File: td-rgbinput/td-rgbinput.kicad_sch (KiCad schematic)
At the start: 52 parts, among them J1 Conn_01x06_Male, J2 Conn_01x07_Male, J3 Conn_01x06_Male, J5 DB15_Female_HighDensity_Mount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, SW1 SW_DIP_x04, U1 TLC272, U11 LM2664M4, U2 ADP7142AUJZ-5.0, U3 ADA4861-3, U4 74HCT00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

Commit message: fix todos
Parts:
- removed U11: LM2664M4, Package_TO_SOT_SMD:SOT-23-6, symbol td-io:LM2664M4
- removed U2: ADP7142AUJZ-5.0, Package_TO_SOT_SMD:TSOT-23-5, symbol Regulator_Linear:ADP7142AUJZ-5.0
- added C? (x3): 0.1uF, Capacitor_SMD:C_0805_2012Metric, symbol Device:C
- added unit 3 of U1
- added U11: MAX1720EUT, Package_TO_SOT_SMD:SOT-23-6, symbol td-io:MAX1720EUT
- added U?: TLC274, symbol Amplifier_Operational:TLC274
- added U?: ADP7142ARDZ-5.0, Package_SO:SOIC-8-1EP_3.9x4.9mm_P1.27mm_EP2.29x3mm, symbol Regulator_Linear:ADP7142ARDZ-5.0
- added U?: 74HCT00, Package_SO:SOIC-14_3.9x8.7mm_P1.27mm, symbol 74xx:74HC00
- SW1: Digikey CT2064-ND -> CT2194MST-ND
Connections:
- net +12V: now also J3.1 (Pin_1), U?.5 (EN), U?.7 (VIN), U?.8 (VIN); no longer J3.6 (Pin_6)
- net +5V: now also C?.1, C?.1, C?.1, U1.8 (V+), U11.2 (V+), U11.5 (SHDN), U?.1 (VOUT), U?.14 (VCC), U?.2 (VOUT), U?.3 (SENSE/ADJ), U?.4 (V+)
- net -5V: now also RV1.3, C?.2, C?.2, U1.4 (V-), U11.1 (OUT), U?.11 (V-)
- net GND: now also J3.5 (Pin_5), J3.6 (Pin_6), C?.2, U11.4 (GND), U?.4 (GND), U?.7 (GND), U?.9 (GND); no longer J3.1 (Pin_1), J3.2 (Pin_2), RV1.3
- net neck_blue: now also J3.4 (Pin_4); no longer J3.3 (Pin_3)
- net neck_green: now also J3.3 (Pin_3); no longer J3.4 (Pin_4)
- net neck_red: now also J3.2 (Pin_2); no longer J3.5 (Pin_5)
- net at C30.2: now also U11.3 (CAP-)
- net at C30.1: now also U11.6 (CAP+)
- no-connect marks 4 -> 5
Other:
- note removed: "todo: switch gain knob to -5V add power to global opamp add power to 7400 change linear regulator footprint reduce paste on ad8337 reverse pinout on output connector switch digikey pn on dip sw"

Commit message: finish pcb
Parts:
- removed C?: 0.1uF, Capacitor_SMD:C_0805_2012Metric, symbol Device:C
- removed R10: 1k, Resistor_SMD:R_0805_2012Metric, symbol Device:R
- removed RV3: 1k, Potentiometer_THT:Potentiometer_Bourns_3386P_Vertical, symbol Device:R_POT
- removed U?: TLC274, symbol Amplifier_Operational:TLC274
- gave numbers to parts that had none: 4

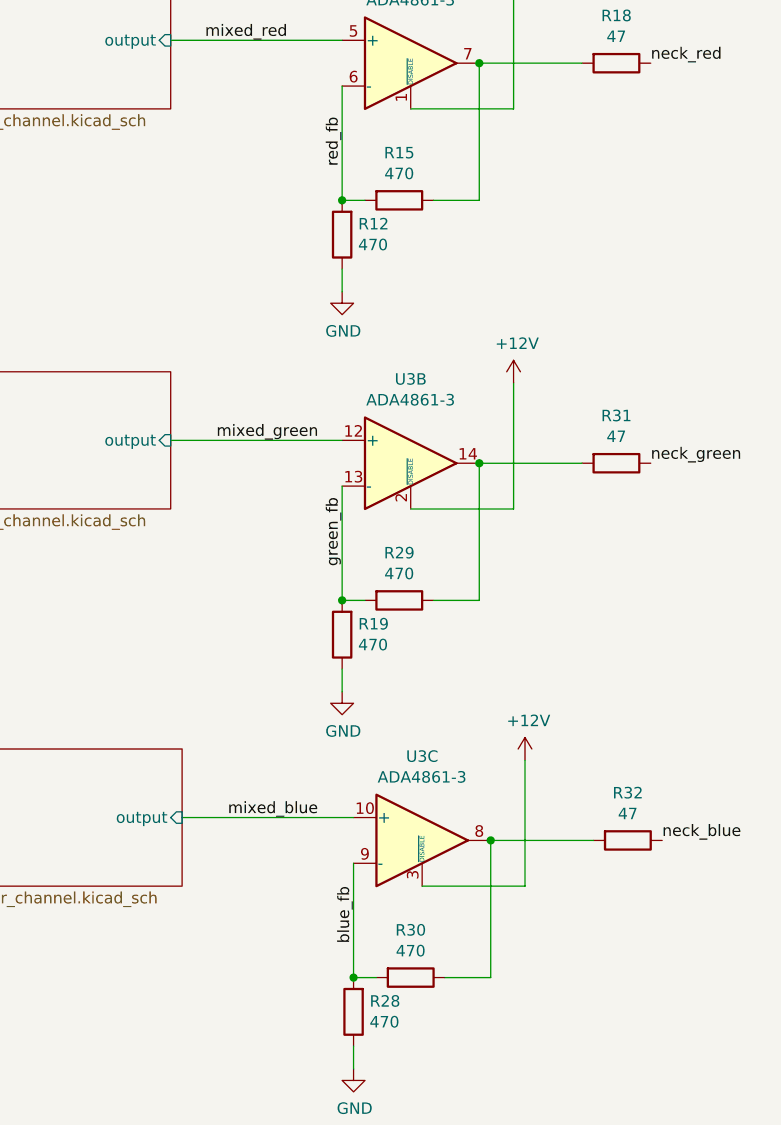
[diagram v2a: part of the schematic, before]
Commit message: update td-rgbinput to reflect constructed circuit
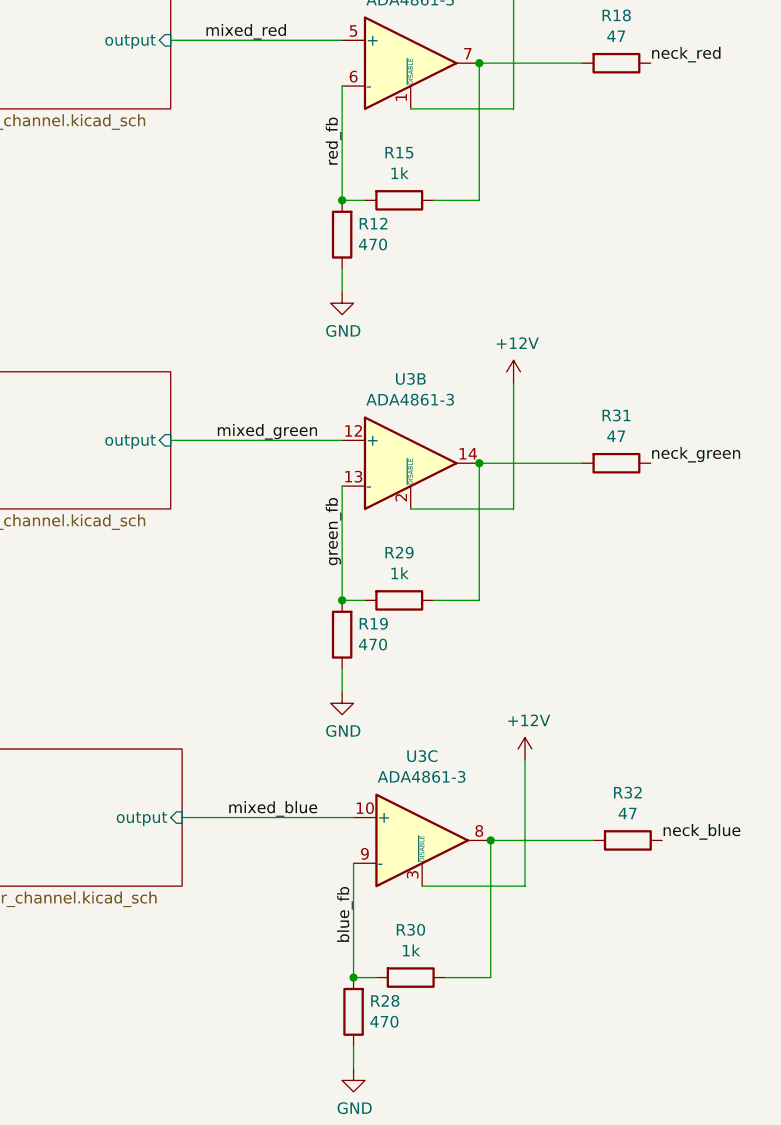
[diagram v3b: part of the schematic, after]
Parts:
- R15, R29, R30: value 470 -> 1k; Digikey YAG3733CT-ND -> (none)
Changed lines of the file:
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@@
     (in_bom yes) (on_board yes)
     (property "Reference" "R15" (id 0) (at 314.96 63.3222 90))
-    (property "Value" "470" (id 1) (at 314.96 65.6336 90))
+    (property "Value" "1k" (id 1) (at 314.96 65.6336 90))
     (property "Footprint" "Resistor_SMD:R_0805_2012Metric" (id 2) (at 314.96 66.802 90)
       (effects (font (size 1.27 1.27)) hide)
@@
       (effects (font (size 1.27 1.27)) hide)
     )
-    (property "Digikey" "YAG3733CT-ND" (id 4) (at 314.96 68.58 0)
+    (property "Digikey" "" (id 4) (at 314.96 68.58 0)
       (effects (font (size 1.27 1.27)) hide)
     )
@@
     (in_bom yes) (on_board yes)
     (property "Reference" "R29" (id 0) (at 314.96 107.7722 90))
-    (property "Value" "470" (id 1) (at 314.96 110.0836 90))
+    (property "Value" "1k" (id 1) (at 314.96 110.0836 90))
     (property "Footprint" "Resistor_SMD:R_0805_2012Metric" (id 2) (at 314.96 111.252 90)
       (effects (font (size 1.27 1.27)) hide)
@@
       (effects (font (size 1.27 1.27)) hide)
     )
-    (property "Digikey" "YAG3733CT-ND" (id 4) (at 314.96 113.03 0)
+    (property "Digikey" "" (id 4) (at 314.96 113.03 0)
       (effects (font (size 1.27 1.27)) hide)
     )
@@
     (in_bom yes) (on_board yes)
     (property "Reference" "R30" (id 0) (at 316.23 149.6822 90))
-    (property "Value" "470" (id 1) (at 316.23 151.9936 90))
+    (property "Value" "1k" (id 1) (at 316.23 151.9936 90))
     (property "Footprint" "Resistor_SMD:R_0805_2012Metric" (id 2) (at 316.23 153.162 90)
       (effects (font (size 1.27 1.27)) hide)
@@
       (effects (font (size 1.27 1.27)) hide)
     )
-    (property "Digikey" "YAG3733CT-ND" (id 4) (at 316.23 154.94 0)
+    (property "Digikey" "" (id 4) (at 316.23 154.94 0)
       (effects (font (size 1.27 1.27)) hide)
     )
@@
       (reference "#PWR0117") (unit 1) (value "+5V") (footprint "")
     )
-    (path "/00000000-0000-0000-0000-0000618fc4a2/9c91e0e5-b30d-4538-ba18-c84d90521e3d"
-      (reference "#PWR0118") (unit 1) (value "GND") (footprint "")
-    )
     (path "/00000000-0000-0000-0000-0000618fc4a2/879ef088-b267-418b-b2b5-0ad6b2a08b53"
       (reference "#PWR0119") (unit 1) (value "+5V") (footprint "")
@@
       (reference "#PWR0129") (unit 1) (value "-5V") (footprint "")
     )
-    (path "/00000000-0000-0000-0000-0000618f5f7a/9c91e0e5-b30d-4538-ba18-c84d90521e3d"
-      (reference "#PWR0130") (unit 1) (value "GND") (footprint "")
-    )
     (path "/00000000-0000-0000-0000-0000618f5f7a/879ef088-b267-418b-b2b5-0ad6b2a08b53"
       (reference "#PWR0131") (unit 1) (value "+5V") (footprint "")
@@
       (reference "#PWR0139") (unit 1) (value "+5V") (footprint "")
     )
-    (path "/00000000-0000-0000-0000-0000618d9864/9c91e0e5-b30d-4538-ba18-c84d90521e3d"
-      (reference "#PWR0140") (unit 1) (value "GND") (footprint "")
-    )
     (path "/00000000-0000-0000-0000-0000618d9864/879ef088-b267-418b-b2b5-0ad6b2a08b53"
       (reference "#PWR0141") (unit 1) (value "+5V") (footprint "")
@@
     )
     (path "/00000000-0000-0000-0000-000060050cff"
-      (reference "R15") (unit 1) (value "470") (footprint "Resistor_SMD:R_0805_2012Metric")
+      (reference "R15") (unit 1) (value "1k") (footprint "Resistor_SMD:R_0805_2012Metric")
     )
     (path "/00000000-0000-0000-0000-0000618d9864/00000000-0000-0000-0000-0000618ebd84"
@@
     )
     (path "/00000000-0000-0000-0000-00006193399d"
-      (reference "R29") (unit 1) (value "470") (footprint "Resistor_SMD:R_0805_2012Metric")
+      (reference "R29") (unit 1) (value "1k") (footprint "Resistor_SMD:R_0805_2012Metric")
     )
     (path "/00000000-0000-0000-0000-00006193a64f"
-      (reference "R30") (unit 1) (value "470") (footprint "Resistor_SMD:R_0805_2012Metric")
+      (reference "R30") (unit 1) (value "1k") (footprint "Resistor_SMD:R_0805_2012Metric")
     )
     (path "/00000000-0000-0000-0000-0000619339b6"
